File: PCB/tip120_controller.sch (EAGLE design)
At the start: 10 parts, among them J1 AUDIO_JACK_3.5MM_PTH, Q1 TIP120, X1 12V

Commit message: silkscreen update
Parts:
- LED1: value RED -> (none)
- PJ-102A, S1: value 12V -> 6-12V
- renumbered X1 to PJ-102A
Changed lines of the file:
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@@
 <?xml version="1.0" encoding="utf-8"?>
 <!DOCTYPE eagle SYSTEM "eagle.dtd">
-<eagle version="8.7.1">
+<eagle version="9.0.0">
 <drawing>
 <settings>
@@
 <part name="U$1" library="SparkFun-Boards" deviceset="ARDUINO_MINI" device=""/>
 <part name="U$2" library="SparkFun-Aesthetics" deviceset="AGND" device=""/>
-<part name="X1" library="con-shiua-chyuan" library_urn="urn:adsk.eagle:library:186" deviceset="SCD-014A" device="" package3d_urn="urn:adsk.eagle:package:10023/1" value="12V"/>
-<part name="S1" library="SparkFun-Switches" deviceset="SWITCH-SPDT" device="-PTH-11.6X4.0MM-KIT" value="12V"/>
+<part name="PJ-102A" library="con-shiua-chyuan" library_urn="urn:adsk.eagle:library:186" deviceset="SCD-014A" device="" package3d_urn="urn:adsk.eagle:package:10023/1" value="6-12V"/>
+<part name="S1" library="SparkFun-Switches" deviceset="SWITCH-SPDT" device="-PTH-11.6X4.0MM-KIT" value="6-12V"/>
 <part name="U$3" library="SparkFun-Aesthetics" deviceset="AGND" device=""/>
 <part name="R2" library="resistor" library_urn="urn:adsk.eagle:library:348" deviceset="R-US_" device="0204/2V" package3d_urn="urn:adsk.eagle:package:25948/1" value="220"/>
-<part name="LED1" library="led" library_urn="urn:adsk.eagle:library:259" deviceset="LED" device="5MM" package3d_urn="urn:adsk.eagle:package:15799/2" value="RED"/>
+<part name="LED1" library="led" library_urn="urn:adsk.eagle:library:259" deviceset="LED" device="5MM" package3d_urn="urn:adsk.eagle:package:15799/2"/>
 <part name="Q1" library="transistor-power" library_urn="urn:adsk.eagle:library:400" deviceset="TIP120" device="" package3d_urn="urn:adsk.eagle:package:29488/1"/>
 <part name="R1" library="resistor" library_urn="urn:adsk.eagle:library:348" deviceset="R-US_" device="0204/2V" package3d_urn="urn:adsk.eagle:package:25948/1" value="2.2k"/>
@@
 <instance part="U$1" gate="G$1" x="55.88" y="40.64"/>
 <instance part="U$2" gate="G$1" x="83.82" y="50.8" rot="R90"/>
-<instance part="X1" gate="G$1" x="78.74" y="78.74" rot="R90"/>
+<instance part="PJ-102A" gate="G$1" x="78.74" y="78.74" rot="R90"/>
 <instance part="S1" gate="1" x="73.66" y="68.58" rot="R270"/>
 <instance part="U$3" gate="G$1" x="33.02" y="63.5" rot="R270"/>
@@
 <pinref part="U$2" gate="G$1" pin="AGND"/>
 <wire x1="68.58" y1="50.8" x2="76.2" y2="50.8" width="0.1524" layer="91"/>
-<pinref part="X1" gate="G$1" pin="3"/>
+<pinref part="PJ-102A" gate="G$1" pin="3"/>
 <wire x1="76.2" y1="50.8" x2="78.74" y2="50.8" width="0.1524" layer="91"/>
 <wire x1="78.74" y1="50.8" x2="81.28" y2="50.8" width="0.1524" layer="91"/>
 <wire x1="78.74" y1="73.66" x2="78.74" y2="68.58" width="0.1524" layer="91"/>
 <wire x1="78.74" y1="68.58" x2="81.28" y2="68.58" width="0.1524" layer="91"/>
-<pinref part="X1" gate="G$1" pin="2"/>
+<pinref part="PJ-102A" gate="G$1" pin="2"/>
 <wire x1="81.28" y1="68.58" x2="81.28" y2="73.66" width="0.1524" layer="91"/>
 <wire x1="78.74" y1="68.58" x2="78.74" y2="50.8" width="0.1524" layer="91"/>
@@
 <net name="N$7" class="0">
 <segment>
-<pinref part="X1" gate="G$1" pin="1"/>
+<pinref part="PJ-102A" gate="G$1" pin="1"/>
 <wire x1="76.2" y1="73.66" x2="76.2" y2="71.12" width="0.1524" layer="91"/>
 <pinref part="S1" gate="1" pin="P"/>

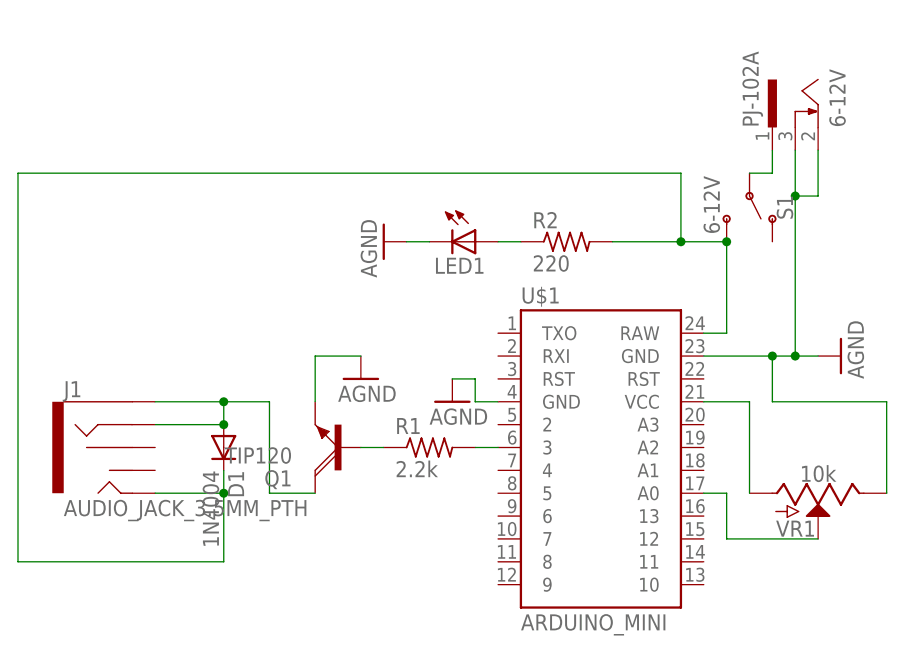
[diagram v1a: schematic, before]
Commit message: replaced transistor symbol/footprint, futzing with silkscreen
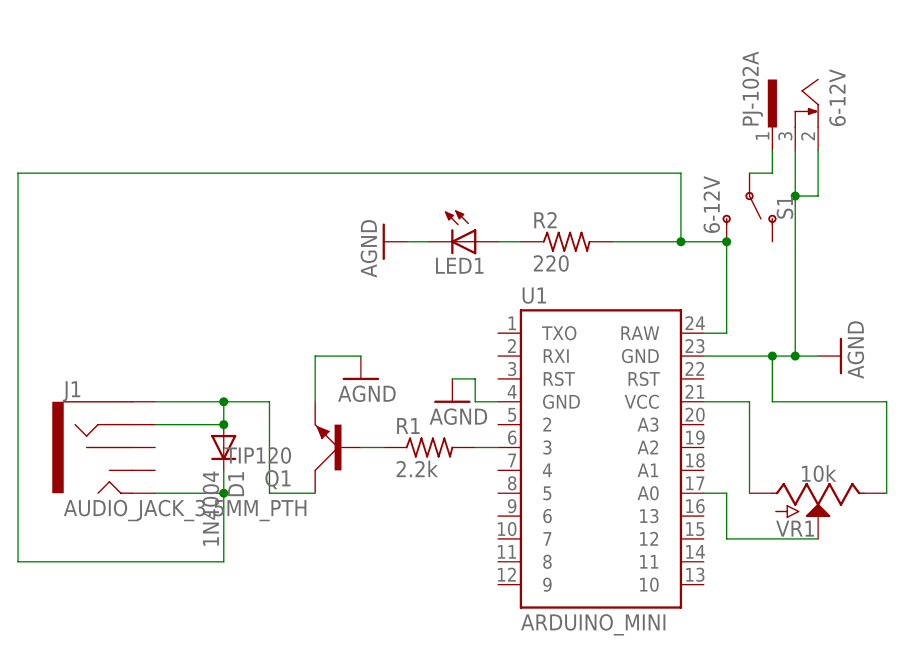
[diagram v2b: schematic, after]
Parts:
- Q1: device transistor-power:TIP120 -> transistor-power:TIP41C
- renumbered U$1 to U1
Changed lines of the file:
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@@
 </classes>
 <parts>
-<part name="U$1" library="SparkFun-Boards" deviceset="ARDUINO_MINI" device=""/>
+<part name="U1" library="SparkFun-Boards" deviceset="ARDUINO_MINI" device=""/>
 <part name="U$2" library="SparkFun-Aesthetics" deviceset="AGND" device=""/>
 <part name="PJ-102A" library="con-shiua-chyuan" library_urn="urn:adsk.eagle:library:186" deviceset="SCD-014A" device="" package3d_urn="urn:adsk.eagle:package:10023/1" value="6-12V"/>
@@
 <part name="R2" library="resistor" library_urn="urn:adsk.eagle:library:348" deviceset="R-US_" device="0204/2V" package3d_urn="urn:adsk.eagle:package:25948/1" value="220"/>
 <part name="LED1" library="led" library_urn="urn:adsk.eagle:library:259" deviceset="LED" device="5MM" package3d_urn="urn:adsk.eagle:package:15799/2"/>
-<part name="Q1" library="transistor-power" library_urn="urn:adsk.eagle:library:400" deviceset="TIP120" device="" package3d_urn="urn:adsk.eagle:package:29488/1"/>
 <part name="R1" library="resistor" library_urn="urn:adsk.eagle:library:348" deviceset="R-US_" device="0204/2V" package3d_urn="urn:adsk.eagle:package:25948/1" value="2.2k"/>
 <part name="U$4" library="SparkFun-Aesthetics" deviceset="AGND" device=""/>
@@
 <part name="VR1" library="SparkFun-Resistors" deviceset="POTENTIOMETER" device="-PTH-9MM-1/20W-20%" value="10k"/>
 <part name="D1" library="diode" library_urn="urn:adsk.eagle:library:210" deviceset="1N4004" device="" package3d_urn="urn:adsk.eagle:package:43336/1"/>
+<part name="Q1" library="transistor-power" library_urn="urn:adsk.eagle:library:400" deviceset="TIP41C" device="" package3d_urn="urn:adsk.eagle:package:29487/2" value="TIP120"/>
 </parts>
 <sheets>
@@
 </plain>
 <instances>
-<instance part="U$1" gate="G$1" x="55.88" y="40.64"/>
+<instance part="U1" gate="G$1" x="55.88" y="40.64"/>
 <instance part="U$2" gate="G$1" x="83.82" y="50.8" rot="R90"/>
 <instance part="PJ-102A" gate="G$1" x="78.74" y="78.74" rot="R90"/>
@@
 <instance part="R2" gate="G$1" x="53.34" y="63.5"/>
 <instance part="LED1" gate="G$1" x="43.18" y="63.5" rot="R270"/>
-<instance part="Q1" gate="1" x="27.94" y="40.64" rot="R180"/>
 <instance part="R1" gate="G$1" x="38.1" y="40.64"/>
 <instance part="U$4" gate="G$1" x="30.48" y="48.26"/>
@@
 <instance part="VR1" gate="G$1" x="81.28" y="35.56" rot="R270"/>
 <instance part="D1" gate="1" x="15.24" y="40.64" rot="R270"/>
+<instance part="Q1" gate="1" x="27.94" y="40.64" rot="R180"/>
 </instances>
 <busses>
@@
 <net name="AGND" class="0">
 <segment>
-<pinref part="U$1" gate="G$1" pin="GND@2"/>
+<pinref part="U1" gate="G$1" pin="GND@2"/>
 <pinref part="U$2" gate="G$1" pin="AGND"/>
 <wire x1="68.58" y1="50.8" x2="76.2" y2="50.8" width="0.1524" layer="91"/>
@@
 <pinref part="U$5" gate="G$1" pin="AGND"/>
 <wire x1="40.64" y1="48.26" x2="43.18" y2="48.26" width="0.1524" layer="91"/>
-<pinref part="U$1" gate="G$1" pin="GND"/>
+<pinref part="U1" gate="G$1" pin="GND"/>
 <wire x1="43.18" y1="48.26" x2="43.18" y2="45.72" width="0.1524" layer="91"/>
 <wire x1="43.18" y1="45.72" x2="45.72" y2="45.72" width="0.1524" layer="91"/>
@@
 </segment>
 </net>
-<net name="N$2" class="0">
-<segment>
-<pinref part="Q1" gate="1" pin="B"/>
-<pinref part="R1" gate="G$1" pin="1"/>
-<wire x1="30.48" y1="40.64" x2="33.02" y2="40.64" width="0.1524" layer="91"/>
-</segment>
-</net>
 <net name="N$8" class="0">
 <segment>
@@
 <wire x1="71.12" y1="63.5" x2="71.12" y2="53.34" width="0.1524" layer="91"/>
 <junction x="71.12" y="63.5"/>
-<pinref part="U$1" gate="G$1" pin="RAW"/>
+<pinref part="U1" gate="G$1" pin="RAW"/>
 <wire x1="71.12" y1="53.34" x2="68.58" y2="53.34" width="0.1524" layer="91"/>
 <wire x1="66.04" y1="63.5" x2="66.04" y2="71.12" width="0.1524" layer="91"/>
@@
 <segment>
 <pinref part="R1" gate="G$1" pin="2"/>
-<pinref part="U$1" gate="G$1" pin="3"/>
+<pinref part="U1" gate="G$1" pin="3"/>
 <wire x1="43.18" y1="40.64" x2="45.72" y2="40.64" width="0.1524" layer="91"/>
 </segment>
@@
 <pinref part="J1" gate="G$1" pin="SLEEVE"/>
 <wire x1="15.24" y1="45.72" x2="7.62" y2="45.72" width="0.1524" layer="91"/>
-<pinref part="Q1" gate="1" pin="C"/>
-<wire x1="25.4" y1="35.56" x2="20.32" y2="35.56" width="0.1524" layer="91"/>
 <wire x1="20.32" y1="35.56" x2="20.32" y2="45.72" width="0.1524" layer="91"/>
 <wire x1="20.32" y1="45.72" x2="15.24" y2="45.72" width="0.1524" layer="91"/>
@@
 <pinref part="D1" gate="1" pin="A"/>
 <junction x="15.24" y="43.18"/>
+<pinref part="Q1" gate="1" pin="C"/>
+<wire x1="20.32" y1="35.56" x2="25.4" y2="35.56" width="0.1524" layer="91"/>
 </segment>
 </net>
 <net name="N$5" class="0">
 <segment>
-<pinref part="U$1" gate="G$1" pin="VCC"/>
+<pinref part="U1" gate="G$1" pin="VCC"/>
 <wire x1="68.58" y1="45.72" x2="73.66" y2="45.72" width="0.1524" layer="91"/>
 <pinref part="VR1" gate="G$1" pin="A"/>
@@
 <wire x1="81.28" y1="30.48" x2="71.12" y2="30.48" width="0.1524" layer="91"/>
 <wire x1="71.12" y1="30.48" x2="71.12" y2="35.56" width="0.1524" layer="91"/>
-<pinref part="U$1" gate="G$1" pin="A0"/>
+<pinref part="U1" gate="G$1" pin="A0"/>
 <wire x1="71.12" y1="35.56" x2="68.58" y2="35.56" width="0.1524" layer="91"/>
 </segment>
 </net>
+<net name="N$2" class="0">
+<segment>
+<pinref part="Q1" gate="1" pin="B"/>
+<pinref part="R1" gate="G$1" pin="1"/>
+<wire x1="30.48" y1="40.64" x2="33.02" y2="40.64" width="0.1524" layer="91"/>
+</segment>
+</net>

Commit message: sanity check
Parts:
- LED1: value (none) -> RED
- S1: value 6-12V -> EG1218
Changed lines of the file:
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@@
 <part name="U$2" library="SparkFun-Aesthetics" deviceset="AGND" device=""/>
 <part name="PJ-102A" library="con-shiua-chyuan" library_urn="urn:adsk.eagle:library:186" deviceset="SCD-014A" device="" package3d_urn="urn:adsk.eagle:package:10023/1" value="6-12V"/>
-<part name="S1" library="SparkFun-Switches" deviceset="SWITCH-SPDT" device="-PTH-11.6X4.0MM-KIT" value="6-12V"/>
 <part name="U$3" library="SparkFun-Aesthetics" deviceset="AGND" device=""/>
 <part name="R2" library="resistor" library_urn="urn:adsk.eagle:library:348" deviceset="R-US_" device="0204/2V" package3d_urn="urn:adsk.eagle:package:25948/1" value="220"/>
-<part name="LED1" library="led" library_urn="urn:adsk.eagle:library:259" deviceset="LED" device="5MM" package3d_urn="urn:adsk.eagle:package:15799/2"/>
+<part name="LED1" library="led" library_urn="urn:adsk.eagle:library:259" deviceset="LED" device="5MM" package3d_urn="urn:adsk.eagle:package:15799/2" value="RED"/>
 <part name="R1" library="resistor" library_urn="urn:adsk.eagle:library:348" deviceset="R-US_" device="0204/2V" package3d_urn="urn:adsk.eagle:package:25948/1" value="2.2k"/>
 <part name="U$4" library="SparkFun-Aesthetics" deviceset="AGND" device=""/>
@@
 <part name="D1" library="diode" library_urn="urn:adsk.eagle:library:210" deviceset="1N4004" device="" package3d_urn="urn:adsk.eagle:package:43336/1"/>
 <part name="Q1" library="transistor-power" library_urn="urn:adsk.eagle:library:400" deviceset="TIP41C" device="" package3d_urn="urn:adsk.eagle:package:29487/2" value="TIP120"/>
+<part name="S1" library="SparkFun-Switches" deviceset="SWITCH-SPDT" device="-PTH-11.6X4.0MM-KIT" value="EG1218"/>
 </parts>
 <sheets>
@@
 <instance part="U$2" gate="G$1" x="83.82" y="50.8" rot="R90"/>
 <instance part="PJ-102A" gate="G$1" x="78.74" y="78.74" rot="R90"/>
-<instance part="S1" gate="1" x="73.66" y="68.58" rot="R270"/>
 <instance part="U$3" gate="G$1" x="33.02" y="63.5" rot="R270"/>
 <instance part="R2" gate="G$1" x="53.34" y="63.5"/>
@@
 <instance part="D1" gate="1" x="15.24" y="40.64" rot="R270"/>
 <instance part="Q1" gate="1" x="27.94" y="40.64" rot="R180"/>
+<instance part="S1" gate="1" x="73.66" y="68.58" rot="R270"/>
 </instances>
 <busses>
@@
 <pinref part="PJ-102A" gate="G$1" pin="1"/>
 <wire x1="76.2" y1="73.66" x2="76.2" y2="71.12" width="0.1524" layer="91"/>
+<wire x1="76.2" y1="71.12" x2="73.66" y2="71.12" width="0.1524" layer="91"/>
 <pinref part="S1" gate="1" pin="P"/>
-<wire x1="76.2" y1="71.12" x2="73.66" y2="71.12" width="0.1524" layer="91"/>
 </segment>
 </net>
 <net name="N$8" class="0">
 <segment>
-<pinref part="S1" gate="1" pin="S"/>
 <pinref part="R2" gate="G$1" pin="2"/>
 <wire x1="71.12" y1="63.5" x2="66.04" y2="63.5" width="0.1524" layer="91"/>
 <wire x1="66.04" y1="63.5" x2="58.42" y2="63.5" width="0.1524" layer="91"/>
 <wire x1="71.12" y1="63.5" x2="71.12" y2="53.34" width="0.1524" layer="91"/>
-<junction x="71.12" y="63.5"/>
 <pinref part="U1" gate="G$1" pin="RAW"/>
 <wire x1="71.12" y1="53.34" x2="68.58" y2="53.34" width="0.1524" layer="91"/>
@@
 <wire x1="15.24" y1="27.94" x2="15.24" y2="35.56" width="0.1524" layer="91"/>
 <junction x="15.24" y="35.56"/>
+<pinref part="S1" gate="1" pin="S"/>
+<junction x="71.12" y="63.5"/>
 </segment>
 </net>

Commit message: swap footprints, update version number
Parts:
- S1: device SparkFun-Switches:SWITCH-SPDT-PTH-11.6X4.0MM-KIT -> SparkFun-Switches:SWITCH-SPDT-PTH-11.6X4.0MM-LOCK
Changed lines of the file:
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@@
 <?xml version="1.0" encoding="utf-8"?>
 <!DOCTYPE eagle SYSTEM "eagle.dtd">
-<eagle version="9.0.0">
+<eagle version="9.0.1">
 <drawing>
 <settings>
@@
 <part name="D1" library="diode" library_urn="urn:adsk.eagle:library:210" deviceset="1N4004" device="" package3d_urn="urn:adsk.eagle:package:43336/1"/>
 <part name="Q1" library="transistor-power" library_urn="urn:adsk.eagle:library:400" deviceset="TIP41C" device="" package3d_urn="urn:adsk.eagle:package:29487/2" value="TIP120"/>
-<part name="S1" library="SparkFun-Switches" deviceset="SWITCH-SPDT" device="-PTH-11.6X4.0MM-KIT" value="EG1218"/>
+<part name="S1" library="SparkFun-Switches" deviceset="SWITCH-SPDT" device="-PTH-11.6X4.0MM-LOCK" value="EG1218"/>
 </parts>
 <sheets>
